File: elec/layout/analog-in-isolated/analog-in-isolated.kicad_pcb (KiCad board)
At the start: 2 copper layers, 23 parts, among them U10 10kΩ ±1% 62.5mW, U12 100nF ±10% 16V X7R, U13 10kΩ ±1% 62.5mW, U14 10kΩ ±1% 62.5mW, U15 1kΩ ±1% 62.5mW, U16 1kΩ ±1% 62.5mW, U17 1µF ±10% 25V X5R, U19 1µF ±10% 25V X5R, U2 1µF ±10% 25V X5R, U20 4.7µF ±10% 10V X5R, U21 10µF ±10% 10V X5R, U3 10kΩ ±1% 62.5mW, U4 10kΩ ±1% 62.5mW, U6 1kΩ ±1% 62.5mW, U7 1kΩ ±1% 62.5mW, U8 100nF ±10% 16V X7R, U9 10kΩ ±1% 62.5mW

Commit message: rebuild all modules
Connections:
- net ADJ_NC renamed out
- D1 pad 2: gnd-1 -> gnd
- U1 pad 1: gnd-1 -> gnd
- U1 pad 3: gnd-1 -> gnd
- U1 pad 9: line-3 -> line-2
- U10 pad 1: line-3 -> line-2
- U11 pad 2: line-2 -> line-3
- U11 pad 4: gnd -> gnd-2
- U11 pad 5: gnd-1 -> gnd
- U11 pad 7: line-3 -> line-2
- U12 pad 2: gnd -> gnd-2
- U14 pad 1: line-2 -> line-3
- U15 pad 2: gnd-1 -> gnd
- U17 pad 1: hv-3 -> hv
- U17 pad 2: gnd-1 -> gnd
- U18 pad 1: hv-3 -> hv
- U18 pad 2: gnd-1 -> gnd
- U18 pad 3: hv-3 -> hv
- U19 pad 2: gnd-1 -> gnd
- U2 pad 2: gnd-1 -> gnd
- U20 pad 1: hv -> hv-3
- U20 pad 2: gnd-2 -> gnd-1
- U21 pad 1: hv-3 -> hv
- U21 pad 2: gnd-1 -> gnd
- U22 pad 1: hv -> hv-3
- U22 pad 2: gnd-2 -> gnd-1
- U22 pad 4: gnd-1 -> gnd
- U22 pad 6: hv-3 -> hv
- U4 pad 1: gnd-1 -> gnd
- U5 pad 4: gnd-1 -> gnd
- U6 pad 2: gnd-1 -> gnd
- U8 pad 2: gnd-1 -> gnd
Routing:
- net gnd: track 6.74 -> 66.3 mm, vias 0 -> 4
- net gnd-1: track 66.3 -> 10.1 mm, vias 4 -> 0
- net hv-3: track 11.1 -> 3.91 mm
- net hv: track 3.91 -> 11.1 mm
- net gnd-2: track 10.1 -> 6.74 mm
- net line-3: track 4.79 -> 1.74 mm
- net line-2: track 1.74 -> 4.79 mm

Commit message: core layout, rebuild modules with compiler updates
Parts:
- U16: value 1kΩ ±1% 62.5mW -> infΩ infW
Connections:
- net out renamed ADJ_NC
- D1 pad 2: gnd -> gnd-1
- U1 pad 1: gnd -> gnd-1
- U1 pad 3: gnd -> gnd-1
- U1 pad 8: hv-1 -> hv-3
- U10 pad 2: hv-1 -> hv-3
- U11 pad 1: hv-2 -> hv-1
- U11 pad 2: line-3 -> line
- U11 pad 3: line -> line-3
- U11 pad 4: gnd-2 -> gnd
- U11 pad 5: gnd -> gnd-1
- U11 pad 8: hv-1 -> hv-3
- U12 pad 1: hv-2 -> hv-1
- U12 pad 2: gnd-2 -> gnd
- U13 pad 1: line -> line-3
- U13 pad 2: hv-2 -> hv-1
- U14 pad 1: line-3 -> line
- U14 pad 2: hv-2 -> hv-1
- U15 pad 2: gnd -> gnd-1
- U16 pad 1: hv-1 -> hv-3
- U17 pad 2: gnd -> gnd-1
- U18 pad 2: gnd -> gnd-1
- U18 pad 5: hv-1 -> hv-3
- U19 pad 1: hv-1 -> hv-3
- U19 pad 2: gnd -> gnd-1
- U2 pad 1: hv-1 -> hv-3
- U2 pad 2: gnd -> gnd-1
- U20 pad 1: hv-3 -> hv-2
- U20 pad 2: gnd-1 -> gnd-2
- U21 pad 2: gnd -> gnd-1
- U22 pad 1: hv-3 -> hv-2
- U22 pad 2: gnd-1 -> gnd-2
- U22 pad 4: gnd -> gnd-1
- U4 pad 1: gnd -> gnd-1
- U5 pad 4: gnd -> gnd-1
- U5 pad 8: hv-1 -> hv-3
- U6 pad 2: gnd -> gnd-1
- U8 pad 1: hv-1 -> hv-3
- U8 pad 2: gnd -> gnd-1
- U9 pad 2: hv-1 -> hv-3
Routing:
- net gnd: track 66.3 -> 6.74 mm, vias 4 -> 0
- net gnd-1: track 10.1 -> 66.3 mm, vias 0 -> 4
- net hv-3: track 3.91 -> 33.2 mm, vias 0 -> 2
- net hv-1: track 33.2 -> 9.73 mm, vias 2 -> 0
- net hv-2: track 9.73 -> 3.91 mm
- net gnd-2: track 6.74 -> 10.1 mm

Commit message: Everything builds
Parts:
- D1: footprint atopile:SOD-123_L2.8-W1.8-LS3.7-RD-5bef17 -> atopile:SMB_L4.6-W3.6-LS5.3-RD-330cb3
- U1: footprint lib:MSOP-10_L3.0-W3.0-P0.50-LS5.0-BL -> atopile:MSOP-10_L3.0-W3.0-P0.50-LS5.0-BL-752175
- U10, U13, U14, U3, U4, U9: value 10kΩ ±1% 62.5mW -> 1kΩ ±1% 62.5mW
- U11: footprint lib:SOIC-8_L4.9-W3.9-P1.27-LS6.0-TL -> atopile:SOIC-8_L4.9-W3.9-P1.27-LS6.0-TL-e13595
- U20: value 4.7µF ±10% 10V X5R -> 4.7µF ±10% 25V X5R; footprint atopile:C0603-bd72f6 -> atopile:C0805-3b2e55
- U21: value 10µF ±10% 10V X5R -> 10µF ±10% 25V X5R; footprint atopile:C0603-bd72f6 -> atopile:C0805-3b2e55
- U5: value (none) -> BW CMRR Ib Vos GBW Iout SR
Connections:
- net ADJ_NC renamed out
- net AIN1 renamed analog_in.adc-line-2
- net AIN2 renamed analog_in.adc-line
- net AIN3 renamed analog_in.adc-line-4
- net ALERT_slash_RDY renamed analog_in.adc-line-3
- net gnd-1 renamed analog_in.adc-line-1
- net inverting renamed inverting_input
- D1 pad 1: cathode -> line-1
- U1 pad 10: line-1 -> line-4
- U1 pad 9: line-2 -> line-5
- U10 pad 1: line-2 -> line-5
- U11 pad 2: line -> line-3
- U11 pad 3: line-3 -> line
- U11 pad 4: gnd -> gnd-2
- U11 pad 6: line-1 -> line-4
- U11 pad 7: line-2 -> line-5
- U12 pad 2: gnd -> gnd-2
- U13 pad 1: line-3 -> line
- U14 pad 1: line -> line-3
- U17 pad 1: hv -> hv-2
- U18 pad 1: hv -> hv-2
- U18 pad 3: hv -> hv-2
- U20 pad 1: hv-2 -> hv
- U20 pad 2: gnd-2 -> gnd
- U21 pad 1: hv -> hv-2
- U22 pad 1: hv-2 -> hv
- U22 pad 2: gnd-2 -> gnd
- U22 pad 6: hv -> hv-2
- U5 pad 3: cathode -> line-1
- U6 pad 1: cathode -> line-1
- U7 pad 1: io -> line-2
- U7 pad 2: cathode -> line-1
- U9 pad 1: line-1 -> line-4
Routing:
- net cathode: track 8.99 -> 0.00 mm
- net hv-2: track 3.91 -> 11.1 mm
- net hv: track 11.1 -> 3.91 mm
- net line-4: track 0.00 -> 5.16 mm
- net line-5: track 0.00 -> 4.79 mm
- net line-2: track 4.79 -> 0.00 mm
- net line-1: track 5.16 -> 8.99 mm
- net gnd-2: track 10.1 -> 6.74 mm
- net gnd: track 6.74 -> 10.1 mm

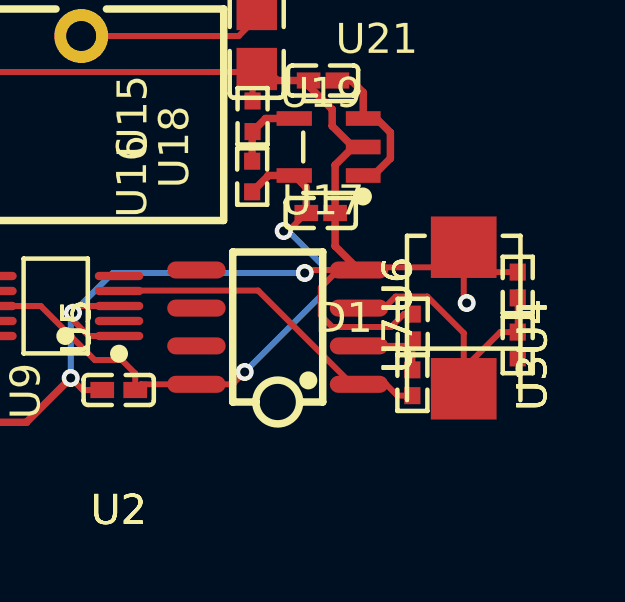
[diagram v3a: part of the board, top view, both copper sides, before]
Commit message: update syntax, delete vendored packages
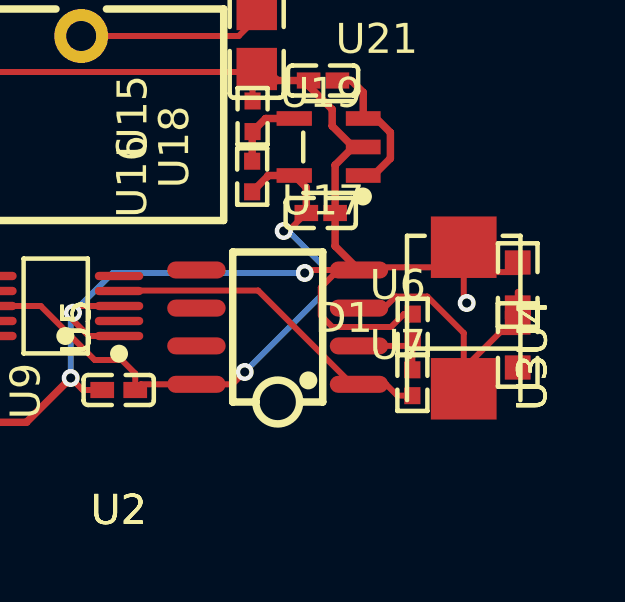
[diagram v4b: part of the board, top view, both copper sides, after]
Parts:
- U10, U13, U14, U15, U3, U4, U9: value 1kΩ ±1% 62.5mW -> 10kΩ ±1% 62.5mW
- U16: value infΩ infW -> 10kΩ ±1% 62.5mW
- U6, U7: value 1kΩ ±1% 62.5mW -> 10kΩ ±1% 100mW; footprint atopile:R0402-56259e -> atopile:R0603-ebcab9
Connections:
- net out renamed ADJ_NC
- D1 pad 1: line-1 -> line-4
- D1 pad 2: analog_in.adc-line-1 -> gnd
- U1 pad 1: analog_in.adc-line-1 -> gnd
- U1 pad 10: line-4 -> line-5
- U1 pad 2: analog_in.adc-line-3 -> analog_in.adc-line-4
- U1 pad 3: analog_in.adc-line-1 -> gnd
- U1 pad 5: analog_in.adc-line-2 -> analog_in.adc-line-3
- U1 pad 6: analog_in.adc-line -> analog_in.adc-line-2
- U1 pad 7: analog_in.adc-line-4 -> analog_in.adc-line-1
- U1 pad 9: line-5 -> line-3
- U10 pad 1: line-5 -> line-3
- U11 pad 2: line-3 -> line-1
- U11 pad 3: line -> line-2
- U11 pad 4: gnd-2 -> gnd-1
- U11 pad 5: analog_in.adc-line-1 -> gnd
- U11 pad 6: line-4 -> line-5
- U11 pad 7: line-5 -> line-3
- U12 pad 2: gnd-2 -> gnd-1
- U13 pad 1: line -> line-2
- U14 pad 1: line-3 -> line-1
- U15 pad 2: analog_in.adc-line-1 -> gnd
- U17 pad 2: analog_in.adc-line-1 -> gnd
- U18 pad 2: analog_in.adc-line-1 -> gnd
- U19 pad 2: analog_in.adc-line-1 -> gnd
- U2 pad 2: analog_in.adc-line-1 -> gnd
- U20 pad 2: gnd -> gnd-2
- U21 pad 2: analog_in.adc-line-1 -> gnd
- U22 pad 2: gnd -> gnd-2
- U22 pad 4: analog_in.adc-line-1 -> gnd
- U4 pad 1: analog_in.adc-line-1 -> gnd
- U5 pad 3: line-1 -> line-4
- U5 pad 4: analog_in.adc-line-1 -> gnd
- U6 pad 1: line-1 -> line-4
- U6 pad 2: analog_in.adc-line-1 -> gnd
- U7 pad 1: line-2 -> line
- U7 pad 2: line-1 -> line-4
- U8 pad 2: analog_in.adc-line-1 -> gnd
- U9 pad 1: line-4 -> line-5
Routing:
- net analog_in.adc-line-1: track 66.3 -> 0.00 mm, vias 4 -> 0
- net gnd: track 10.1 -> 66.3 mm, vias 0 -> 4
- net line-1: track 8.99 -> 1.74 mm
- net gnd-1: track 0.00 -> 6.74 mm
- net line-4: track 5.16 -> 8.99 mm
- net gnd-2: track 6.74 -> 10.1 mm
- net line-3: track 1.74 -> 4.79 mm
- net line-2: track 0.00 -> 1.61 mm
- net line: track 1.61 -> 0.00 mm
